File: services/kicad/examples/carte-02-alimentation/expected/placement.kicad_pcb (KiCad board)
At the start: 2 copper layers, 55 x 40 mm, 12 parts, among them J1 IN_5V, J2 OUT, U1 AMS1117-3.3, U2 AMS1117-1.8

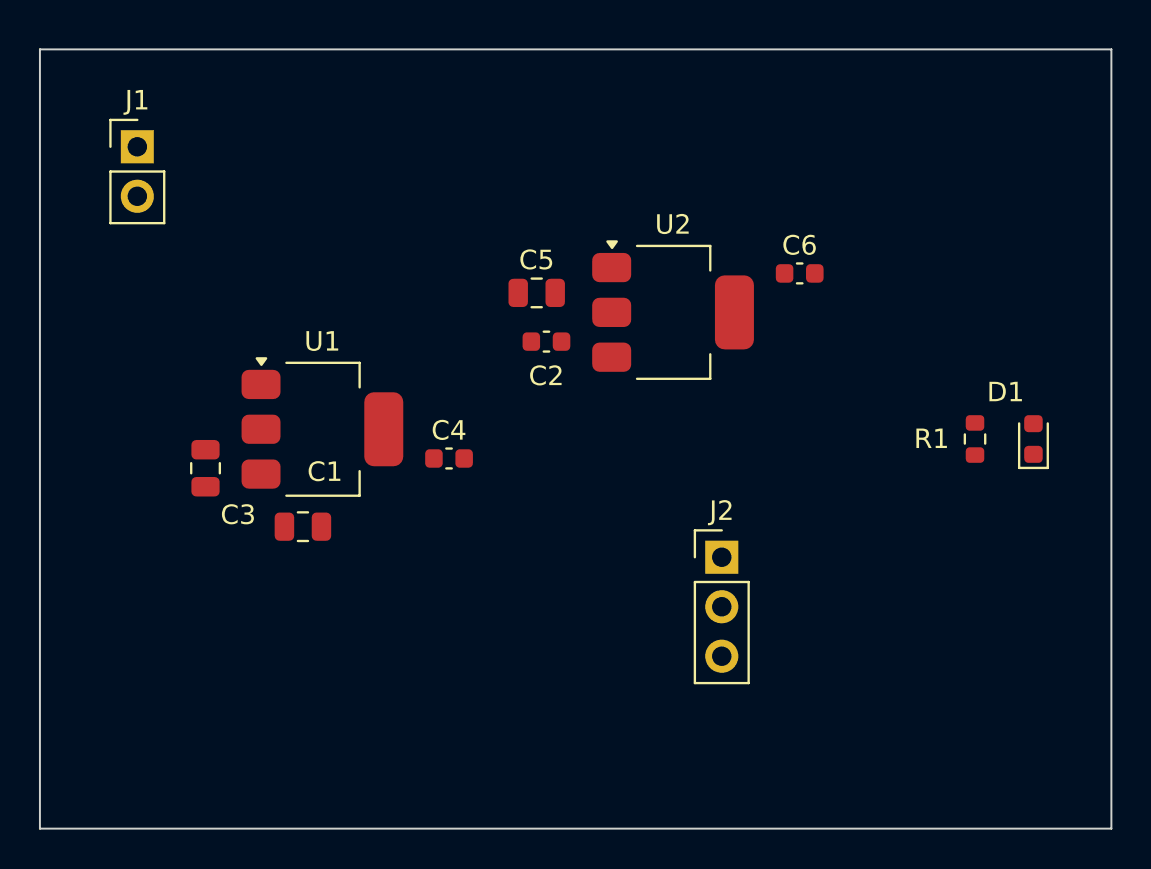
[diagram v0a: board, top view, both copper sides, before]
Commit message: chore(banc): relivrer carte-01/02/04/05 compactes (25 %, D-2026-09-20-a) (#222)
Chaine place -> route rejouee par HTTP sur les dix cartes avec le code de
#220/#221. Quatre sortent a 0 erreur et 0 connexion manquante, sur des
cartes 18 a 58 % plus petites :

  carte-01  24,8x17 -> 20x14      carte-02  55x40 -> 35x25
  carte-04  45x44,8 -> 39x30      carte-05  70x50 -> 46x33

placement.kicad_pcb et final.kicad_pcb remplaces ENSEMBLE ; mesures.json :
board recompte, drc_du_board rejuge (remesurer_banc.py), cle
carte_compacte (tailles et vias d avant, durees, moteur, pistes par
couche). Rendus refaits. Connecteurs a <= 5 mm d un bord (carte-02 J2 :
13,9 -> 3,8 mm) ; carte-05 J3 inchange a 11,4 mm (origine pin 1).

Les six autres gardent leur board du 2026-09-19 : 06 et 08 a 1 manquante,
03 et 07 mauvais, 09 et 10 sans board (tirages figes). Detail dans
BANC_DRIVER_LLM.md. carte-11 non touchee.


Claude-Session: https://claude.ai/code/session_01TnMqm4La2CxQHHB5K8aSSV

Co-authored-by: Claude Fable 5.1 <noreply@anthropic.com>
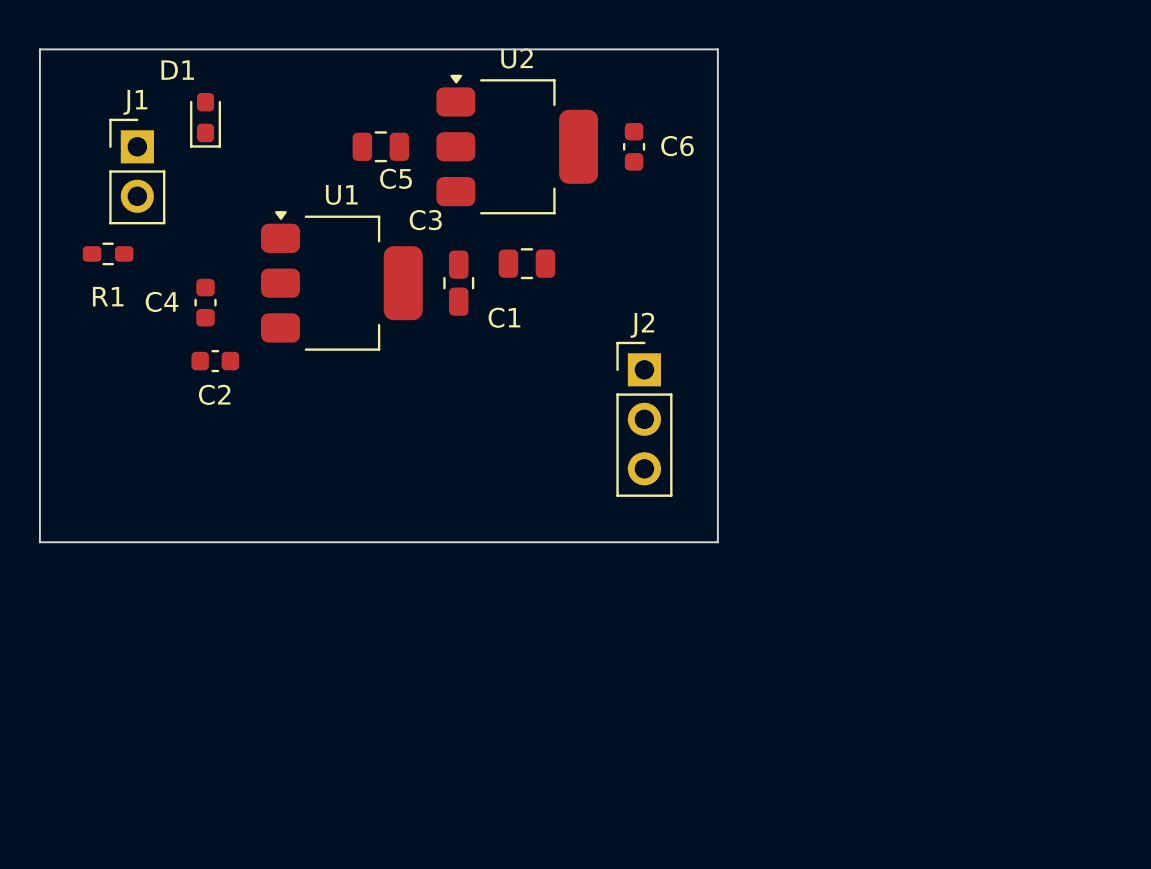
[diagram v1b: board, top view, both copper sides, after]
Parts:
- moved D1 45.6 mm to (129.5, 88.5)
- moved R1 45.5 mm to (124.5, 95.5), turned to 180 degrees
- moved C1 17.7 mm to (146.0, 96.0), turned to 180 degrees
- moved C2 17.0 mm to (130.0, 101.0)
- moved C3 16.1 mm to (142.5, 97.0), turned to 90 degrees
- moved C4 14.8 mm to (129.5, 98.0), turned to 90 degrees
- moved U2 11.7 mm to (145.5, 90.0)
- moved C5 11.0 mm to (138.5, 90.0), turned to 180 degrees
- moved C6 10.7 mm to (151.5, 90.0), turned to 270 degrees
- moved J2 10.4 mm to (152.0, 101.5)
- moved U1 7.57 mm to (136.5, 97.0)
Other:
- board size 55 x 40 mm -> 34.8 x 25.3 mm
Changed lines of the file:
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@@
 	(net 4 "VIN")
 	(net 5 "LED_A")
-	(gr_rect
-		(start 121 85)
-		(end 176 125)
-		(stroke
-			(width 0.1)
-			(type default)
-		)
-		(fill none)
-		(layer "Edge.Cuts")
-	)
 	(footprint "PinHeader_1x02_P2.54mm_Vertical"
 		(version 20260206)
@@
 		(generator_version "10.0")
 		(layer "F.Cu")
-		(at 135.5 104.5 0)
+		(at 136.5 97 0)
 		(descr "module CMS SOT223 4 pins")
 		(tags "CMS SOT")
@@
 		(generator_version "10.0")
 		(layer "F.Cu")
-		(at 153.5 98.5 0)
+		(at 145.5 90 0)
 		(descr "module CMS SOT223 4 pins")
 		(tags "CMS SOT")
@@
 		(generator "kicad-footprint-generator")
 		(layer "F.Cu")
-		(at 134.5 109.5 0)
+		(at 146 96 180)
 		(descr "Capacitor SMD 0805 (2012 Metric), square (rectangular) end terminal, IPC-7351 nominal, (Body size source: IPC-SM-782 page 76, https://www.pcb-3d.com/wordpress/wp-content/uploads/ipc-sm-782a_amendment_1_and_2.pdf, https://docs.google.com/spreadsheets/d/1BsfQQcO9C6DZCsRaXUlFlo91Tg2WpOkGARC1WS5S8t0/edit?usp=sharing)")
 		(tags "capacitor")
@@
 		)
 		(pad "1" smd roundrect
-			(at -0.95 0)
+			(at -0.95 0 180)
 			(size 1 1.45)
 			(layers "F.Cu" "F.Mask" "F.Paste")
@@
 		)
 		(pad "2" smd roundrect
-			(at 0.95 0)
+			(at 0.95 0 180)
 			(size 1 1.45)
 			(layers "F.Cu" "F.Mask" "F.Paste")
@@
 		(generator "kicad-footprint-generator")
 		(layer "F.Cu")
-		(at 147 100 0)
+		(at 130 101 0)
 		(descr "Capacitor SMD 0603 (1608 Metric), square (rectangular) end terminal, IPC-7351 nominal, (Body size source: IPC-SM-782 page 76, https://www.pcb-3d.com/wordpress/wp-content/uploads/ipc-sm-782a_amendment_1_and_2.pdf)")
 		(tags "capacitor")
@@
 		(generator "kicad-footprint-generator")
 		(layer "F.Cu")
-		(at 129.5 106.5 270)
+		(at 142.5 97 90)
 		(descr "Capacitor SMD 0805 (2012 Metric), square (rectangular) end terminal, IPC-7351 nominal, (Body size source: IPC-SM-782 page 76, https://www.pcb-3d.com/wordpress/wp-content/uploads/ipc-sm-782a_amendment_1_and_2.pdf, https://docs.google.com/spreadsheets/d/1BsfQQcO9C6DZCsRaXUlFlo91Tg2WpOkGARC1WS5S8t0/edit?usp=sharing)")
 		(tags "capacitor")
 		(property "Reference" "C3"
-			(at 2.4 -1.68 0)
+			(at 3.2 -1.68 0)
 			(layer "F.SilkS")
 			(effects
@@
 		)
 		(pad "1" smd roundrect
-			(at -0.95 0 270)
+			(at -0.95 0)
 			(size 1 1.45)
 			(layers "F.Cu" "F.Mask" "F.Paste")
@@
 		)
 		(pad "2" smd roundrect
-			(at 0.95 0 270)
+			(at 0.95 0)
 			(size 1 1.45)
 			(layers "F.Cu" "F.Mask" "F.Paste")
@@
 		(generator "kicad-footprint-generator")
 		(layer "F.Cu")
-		(at 142 106 0)
+		(at 129.5 98 90)
 		(descr "Capacitor SMD 0603 (1608 Metric), square (rectangular) end terminal, IPC-7351 nominal, (Body size source: IPC-SM-782 page 76, https://www.pcb-3d.com/wordpress/wp-content/uploads/ipc-sm-782a_amendment_1_and_2.pdf)")
 		(tags "capacitor")
 		(property "Reference" "C4"
-			(at 0 -1.43 0)
+			(at -1.46958e-16 -2.23 0)
 			(layer "F.SilkS")
 			(effects
@@
 		)
 		(pad "1" smd roundrect
-			(at -0.775 0)
+			(at -0.775 0 90)
 			(size 0.9 0.95)
 			(layers "F.Cu" "F.Mask" "F.Paste")
@@
 		)
 		(pad "2" smd roundrect
-			(at 0.775 0)
+			(at 0.775 0 90)
 			(size 0.9 0.95)
 			(layers "F.Cu" "F.Mask" "F.Paste")
@@
 		(generator "kicad-footprint-generator")
 		(layer "F.Cu")
-		(at 146.5 97.5 0)
+		(at 138.5 90 180)
 		(descr "Capacitor SMD 0805 (2012 Metric), square (rectangular) end terminal, IPC-7351 nominal, (Body size source: IPC-SM-782 page 76, https://www.pcb-3d.com/wordpress/wp-content/uploads/ipc-sm-782a_amendment_1_and_2.pdf, https://docs.google.com/spreadsheets/d/1BsfQQcO9C6DZCsRaXUlFlo91Tg2WpOkGARC1WS5S8t0/edit?usp=sharing)")
 		(tags "capacitor")
 		(property "Reference" "C5"
-			(at 0 -1.68 0)
+			(at -0.8 -1.68 0)
 			(layer "F.SilkS")
 			(effects
@@
 		)
 		(pad "1" smd roundrect
-			(at -0.95 0)
+			(at -0.95 0 180)
 			(size 1 1.45)
 			(layers "F.Cu" "F.Mask" "F.Paste")
@@
 		)
 		(pad "2" smd roundrect
-			(at 0.95 0)
+			(at 0.95 0 180)
 			(size 1 1.45)
 			(layers "F.Cu" "F.Mask" "F.Paste")
@@
 		(generator "kicad-footprint-generator")
 		(layer "F.Cu")
-		(at 160 96.5 0)
+		(at 151.5 90 270)
 		(descr "Capacitor SMD 0603 (1608 Metric), square (rectangular) end terminal, IPC-7351 nominal, (Body size source: IPC-SM-782 page 76, https://www.pcb-3d.com/wordpress/wp-content/uploads/ipc-sm-782a_amendment_1_and_2.pdf)")
 		(tags "capacitor")
 		(property "Reference" "C6"
-			(at 0 -1.43 0)
+			(at -1.46958e-16 -2.23 0)
 			(layer "F.SilkS")
 			(effects
@@
 		)
 		(pad "1" smd roundrect
-			(at -0.775 0)
+			(at -0.775 0 270)
 			(size 0.9 0.95)
 			(layers "F.Cu" "F.Mask" "F.Paste")
@@
 		)
 		(pad "2" smd roundrect
-			(at 0.775 0)
+			(at 0.775 0 270)
 			(size 0.9 0.95)
 			(layers "F.Cu" "F.Mask" "F.Paste")
@@
 		(generator "kicad-footprint-generator")
 		(layer "F.Cu")
-		(at 169 105 90)
+		(at 124.5 95.5 180)
 		(descr "Resistor SMD 0603 (1608 Metric), square (rectangular) end terminal, IPC-7351 nominal, (Body size source: IPC-SM-782 page 72, https://www.pcb-3d.com/wordpress/wp-content/uploads/ipc-sm-782a_amendment_1_and_2.pdf)")
 		(tags "resistor")
@@
 		)
 		(pad "1" smd roundrect
-			(at -0.825 0 90)
+			(at -0.825 0 270)
 			(size 0.8 0.95)
 			(layers "F.Cu" "F.Mask" "F.Paste")
@@
 		)
 		(pad "2" smd roundrect
-			(at 0.825 0 90)
+			(at 0.825 0 270)
 			(size 0.8 0.95)
 			(layers "F.Cu" "F.Mask" "F.Paste")
@@
 		(generator "kicad-footprint-generator")
 		(layer "F.Cu")
-		(at 172 105 90)
+		(at 129.5 88.5 90)
 		(descr "LED SMD 0603 (1608 Metric), square (rectangular) end terminal, IPC-7351 nominal, (Body size source: http://www.tortai-tech.com/upload/download/2011102023233369053.pdf)")
 		(tags "LED")
@@
 		)
 		(pad "1" smd roundrect
-			(at -0.7875 0 90)
+			(at -0.7875 0 180)
 			(size 0.875 0.95)
 			(layers "F.Cu" "F.Mask" "F.Paste")
@@
 		)
 		(pad "2" smd roundrect
-			(at 0.7875 0 90)
+			(at 0.7875 0 180)
 			(size 0.875 0.95)
 			(layers "F.Cu" "F.Mask" "F.Paste")
@@
 		(generator "kicad-footprint-generator")
 		(layer "F.Cu")
-		(at 156 111.07 0)
+		(at 152.03 101.45 0)
 		(descr "Through hole straight pin header, 1x03, 2.54mm pitch, single row")
 		(tags "Through hole pin header THT 1x03 2.54mm single row")
@@
 		)
 	)
+	(gr_rect
+		(start 121.0 85.0)
+		(end 155.8 110.3)
+		(stroke
+			(width 0.1)
+			(type default)
+		)
+		(fill no)
+		(layer "Edge.Cuts")
+	)
 )
